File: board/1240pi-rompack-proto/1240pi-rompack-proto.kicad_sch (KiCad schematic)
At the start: 0 parts

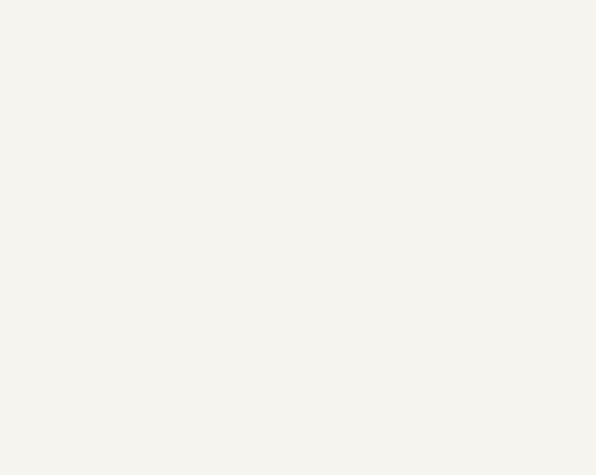
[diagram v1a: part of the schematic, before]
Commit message: Add 3.3v regulator.
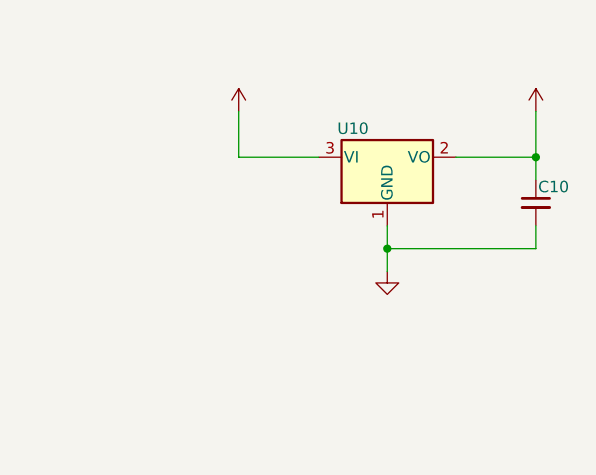
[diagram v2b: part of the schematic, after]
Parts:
- added C10: (no value), symbol Device:C_Small
- added U10: (no value), symbol Regulator_Linear:AMS1117-3.3
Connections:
- new net +3V3: C10.1, U10.2 (VO)
- new net +5V: U10.3 (VI)
- new net GND: C10.2, U10.1 (GND)
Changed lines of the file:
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@@
     (comment 1 "https://github.com/Elemecca/1240pi")
+  )
+  (junction (at 232.41 50.8) (diameter 0) (color 0 0 0 0)
+  )
+  (junction (at 215.9 60.96) (diameter 0) (color 0 0 0 0)
+  )
+  (wire (pts (xy 232.41 60.96) (xy 215.9 60.96))
+    (stroke (width 0) (type default) (color 0 0 0 0))
+  )
+  (wire (pts (xy 232.41 50.8) (xy 232.41 45.72))
+    (stroke (width 0) (type default) (color 0 0 0 0))
+  )
+  (wire (pts (xy 215.9 60.96) (xy 215.9 63.5))
+    (stroke (width 0) (type default) (color 0 0 0 0))
+  )
+  (wire (pts (xy 215.9 58.42) (xy 215.9 60.96))
+    (stroke (width 0) (type default) (color 0 0 0 0))
+  )
+  (wire (pts (xy 199.39 45.72) (xy 199.39 50.8))
+    (stroke (width 0) (type default) (color 0 0 0 0))
+  )
+  (wire (pts (xy 232.41 50.8) (xy 232.41 53.34))
+    (stroke (width 0) (type default) (color 0 0 0 0))
+  )
+  (wire (pts (xy 232.41 58.42) (xy 232.41 60.96))
+    (stroke (width 0) (type default) (color 0 0 0 0))
+  )
+  (wire (pts (xy 199.39 50.8) (xy 208.28 50.8))
+    (stroke (width 0) (type default) (color 0 0 0 0))
+  )
+  (wire (pts (xy 223.52 50.8) (xy 232.41 50.8))
+    (stroke (width 0) (type default) (color 0 0 0 0))
+  )
+  (symbol (lib_id "Device:C_Small") (at 232.41 55.88 0) (unit 1)
+    (in_bom yes) (on_board yes)
+    (property "Reference" "C10" (id 0) (at 232.664 54.102 0)
+      (effects (font (size 1.27 1.27)) (justify left))
+    )
+    (property "Value" "" (id 1) (at 232.664 57.912 0)
+      (effects (font (size 1.27 1.27)) (justify left))
+    )
+    (property "Footprint" "" (id 2) (at 232.41 55.88 0)
+      (effects (font (size 1.27 1.27)) hide)
+    )
+    (property "Datasheet" "~" (id 3) (at 232.41 55.88 0)
+      (effects (font (size 1.27 1.27)) hide)
+    )
+    (pin "1")
+    (pin "2")
+  )
+  (symbol (lib_id "power:+3V3") (at 232.41 45.72 0) (unit 1)
+    (in_bom yes) (on_board yes)
+    (property "Reference" "#PWR0173" (id 0) (at 232.41 49.53 0)
+      (effects (font (size 1.27 1.27)) hide)
+    )
+    (property "Value" "" (id 1) (at 232.41 42.164 0))
+    (property "Footprint" "" (id 2) (at 232.41 45.72 0)
+      (effects (font (size 1.27 1.27)) hide)
+    )
+    (property "Datasheet" "" (id 3) (at 232.41 45.72 0)
+      (effects (font (size 1.27 1.27)) hide)
+    )
+    (pin "1")
+  )
+  (symbol (lib_id "power:+5V") (at 199.39 45.72 0) (unit 1)
+    (in_bom yes) (on_board yes)
+    (property "Reference" "#PWR0171" (id 0) (at 199.39 49.53 0)
+      (effects (font (size 1.27 1.27)) hide)
+    )
+    (property "Value" "" (id 1) (at 199.39 42.164 0))
+    (property "Footprint" "" (id 2) (at 199.39 45.72 0)
+      (effects (font (size 1.27 1.27)) hide)
+    )
+    (property "Datasheet" "" (id 3) (at 199.39 45.72 0)
+      (effects (font (size 1.27 1.27)) hide)
+    )
+    (pin "1")
+  )
+  (symbol (lib_id "power:GND") (at 215.9 63.5 0) (unit 1)
+    (in_bom yes) (on_board yes)
+    (property "Reference" "#PWR0172" (id 0) (at 215.9 69.85 0)
+      (effects (font (size 1.27 1.27)) hide)
+    )
+    (property "Value" "" (id 1) (at 215.9 67.31 0))
+    (property "Footprint" "" (id 2) (at 215.9 63.5 0)
+      (effects (font (size 1.27 1.27)) hide)
+    )
+    (property "Datasheet" "" (id 3) (at 215.9 63.5 0)
+      (effects (font (size 1.27 1.27)) hide)
+    )
+    (pin "1")
+  )
+  (symbol (lib_id "Regulator_Linear:AMS1117-3.3") (at 215.9 50.8 0) (unit 1)
+    (in_bom yes) (on_board yes)
+    (property "Reference" "U10" (id 0) (at 212.09 47.625 0))
+    (property "Value" "" (id 1) (at 215.9 47.625 0)
+      (effects (font (size 1.27 1.27)) (justify left))
+    )
+    (property "Footprint" "" (id 2) (at 215.9 45.72 0)
+      (effects (font (size 1.27 1.27)) hide)
+    )
+    (property "Datasheet" "http://www.advanced-monolithic.com/pdf/ds1117.pdf" (id 3) (at 218.44 57.15 0)
+      (effects (font (size 1.27 1.27)) hide)
+    )
+    (pin "1")
+    (pin "2")
+    (pin "3")
   )
   (sheet (at 101.6 38.1) (size 38.1 25.4) (fields_autoplaced)
@@
       (reference "#PWR0170") (unit 1) (value "+3V3") (footprint "")
     )
+    (path "/bdf90bb5-e826-4d97-8caf-6acc8c57e8e3"
+      (reference "#PWR0171") (unit 1) (value "+5V") (footprint "")
+    )
+    (path "/cd7ecca6-c8cf-4493-b4e5-e53750c35967"
+      (reference "#PWR0172") (unit 1) (value "GND") (footprint "")
+    )
+    (path "/7a42ab4d-dd9d-464d-9dfd-4310c5226a12"
+      (reference "#PWR0173") (unit 1) (value "+3V3") (footprint "")
+    )
+    (path "/c94ef528-8972-4ef9-a49e-b78b8aa291c0/8923add6-1c6c-43e0-a11c-a639f35c2bbc"
+      (reference "#PWR0174") (unit 1) (value "GND") (footprint "")
+    )
+    (path "/c94ef528-8972-4ef9-a49e-b78b8aa291c0/0a28bb2b-cea5-44ba-bfc7-c5ebd7a3e850"
+      (reference "#PWR0175") (unit 1) (value "+3V3") (footprint "")
+    )
+    (path "/c94ef528-8972-4ef9-a49e-b78b8aa291c0/f7c84ccb-c958-489f-b9b7-d99c37d81956"
+      (reference "#PWR0176") (unit 1) (value "+3V3") (footprint "")
+    )
+    (path "/c94ef528-8972-4ef9-a49e-b78b8aa291c0/f912e46a-4940-4e73-8439-3ed3a51f5e1e"
+      (reference "#PWR0177") (unit 1) (value "GND") (footprint "")
+    )
+    (path "/0453f5e9-e8a5-4709-8ddb-dd9b099ed3b3"
+      (reference "C10") (unit 1) (value "22u") (footprint "Capacitor_SMD:C_0805_2012Metric")
+    )
     (path "/b09362f0-138c-401c-8136-03cd8118b133/f9da80db-6b97-4641-a46a-6d8b6da9dad8"
       (reference "C20") (unit 1) (value "2u2") (footprint "Capacitor_SMD:C_0603_1608Metric")
@@
       (reference "C34") (unit 1) (value "2u2") (footprint "Capacitor_SMD:C_0603_1608Metric")
     )
+    (path "/c94ef528-8972-4ef9-a49e-b78b8aa291c0/56d86140-0c89-4b2a-b43d-a5e44eba7d6c"
+      (reference "C35") (unit 1) (value "2u2") (footprint "Capacitor_SMD:C_0603_1608Metric")
+    )
+    (path "/c94ef528-8972-4ef9-a49e-b78b8aa291c0/28094c46-74f8-4da2-ade9-eadf08683e0a"
+      (reference "C36") (unit 1) (value "2u2") (footprint "Capacitor_SMD:C_0603_1608Metric")
+    )
     (path "/b09362f0-138c-401c-8136-03cd8118b133/7bc3bbf6-07f1-4929-b00e-cab5dae43579"
       (reference "J20") (unit 1) (value "CardEdge_ROMPACK") (footprint "0Local:CardEdge_18x2")
@@
       (reference "R32") (unit 1) (value "10k") (footprint "Resistor_SMD:R_0603_1608Metric")
     )
+    (path "/e9d62a37-0d77-44a7-87ad-6c10c7a0c71a"
+      (reference "U10") (unit 1) (value "AMS1117-3.3") (footprint "Package_TO_SOT_SMD:SOT-223-3_TabPin2")
+    )
     (path "/b09362f0-138c-401c-8136-03cd8118b133/81b2411e-06b8-4c49-8e9f-e485eabde5f6"

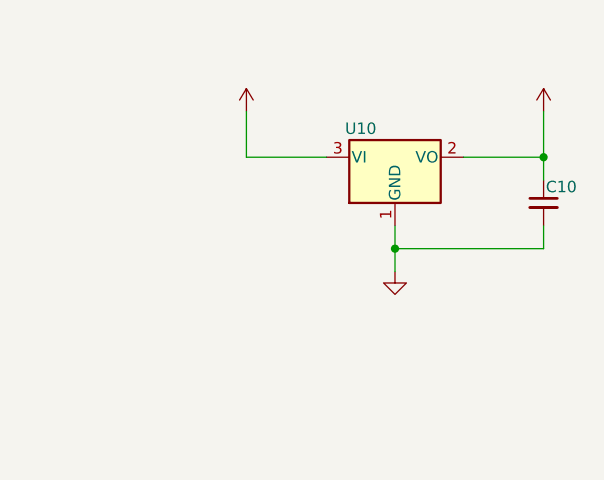
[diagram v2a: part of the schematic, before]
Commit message: Fix names of BUSRQ and IORQ nets.
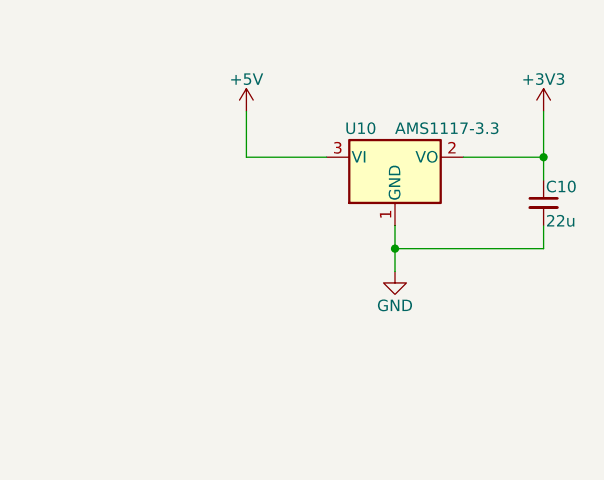
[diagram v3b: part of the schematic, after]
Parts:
- C10: value (none) -> 22u; footprint (none) -> Capacitor_SMD:C_0805_2012Metric
- U10: value (none) -> AMS1117-3.3; footprint (none) -> Package_TO_SOT_SMD:SOT-223-3_TabPin2
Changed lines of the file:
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@@
       (effects (font (size 1.27 1.27)) (justify left))
     )
-    (property "Value" "" (id 1) (at 232.664 57.912 0)
+    (property "Value" "22u" (id 1) (at 232.664 57.912 0)
       (effects (font (size 1.27 1.27)) (justify left))
     )
-    (property "Footprint" "" (id 2) (at 232.41 55.88 0)
+    (property "Footprint" "Capacitor_SMD:C_0805_2012Metric" (id 2) (at 232.41 55.88 0)
       (effects (font (size 1.27 1.27)) hide)
     )
@@
       (effects (font (size 1.27 1.27)) hide)
     )
-    (property "Value" "" (id 1) (at 232.41 42.164 0))
+    (property "Value" "+3V3" (id 1) (at 232.41 42.164 0))
     (property "Footprint" "" (id 2) (at 232.41 45.72 0)
       (effects (font (size 1.27 1.27)) hide)
@@
       (effects (font (size 1.27 1.27)) hide)
     )
-    (property "Value" "" (id 1) (at 199.39 42.164 0))
+    (property "Value" "+5V" (id 1) (at 199.39 42.164 0))
     (property "Footprint" "" (id 2) (at 199.39 45.72 0)
       (effects (font (size 1.27 1.27)) hide)
@@
       (effects (font (size 1.27 1.27)) hide)
     )
-    (property "Value" "" (id 1) (at 215.9 67.31 0))
+    (property "Value" "GND" (id 1) (at 215.9 67.31 0))
     (property "Footprint" "" (id 2) (at 215.9 63.5 0)
       (effects (font (size 1.27 1.27)) hide)
@@
     (in_bom yes) (on_board yes)
     (property "Reference" "U10" (id 0) (at 212.09 47.625 0))
-    (property "Value" "" (id 1) (at 215.9 47.625 0)
+    (property "Value" "AMS1117-3.3" (id 1) (at 215.9 47.625 0)
       (effects (font (size 1.27 1.27)) (justify left))
     )
-    (property "Footprint" "" (id 2) (at 215.9 45.72 0)
+    (property "Footprint" "Package_TO_SOT_SMD:SOT-223-3_TabPin2" (id 2) (at 215.9 45.72 0)
       (effects (font (size 1.27 1.27)) hide)
     )
